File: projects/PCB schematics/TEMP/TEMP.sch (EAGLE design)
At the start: 58 parts, among them J1 SAMTEC-TFM-120-02-X-D-LCJ, J2 SAMTEC-TFM-120-02-X-D-LCJ, X1 5566-2, X2 5566-4, X3 5566-6, X4 5566-4

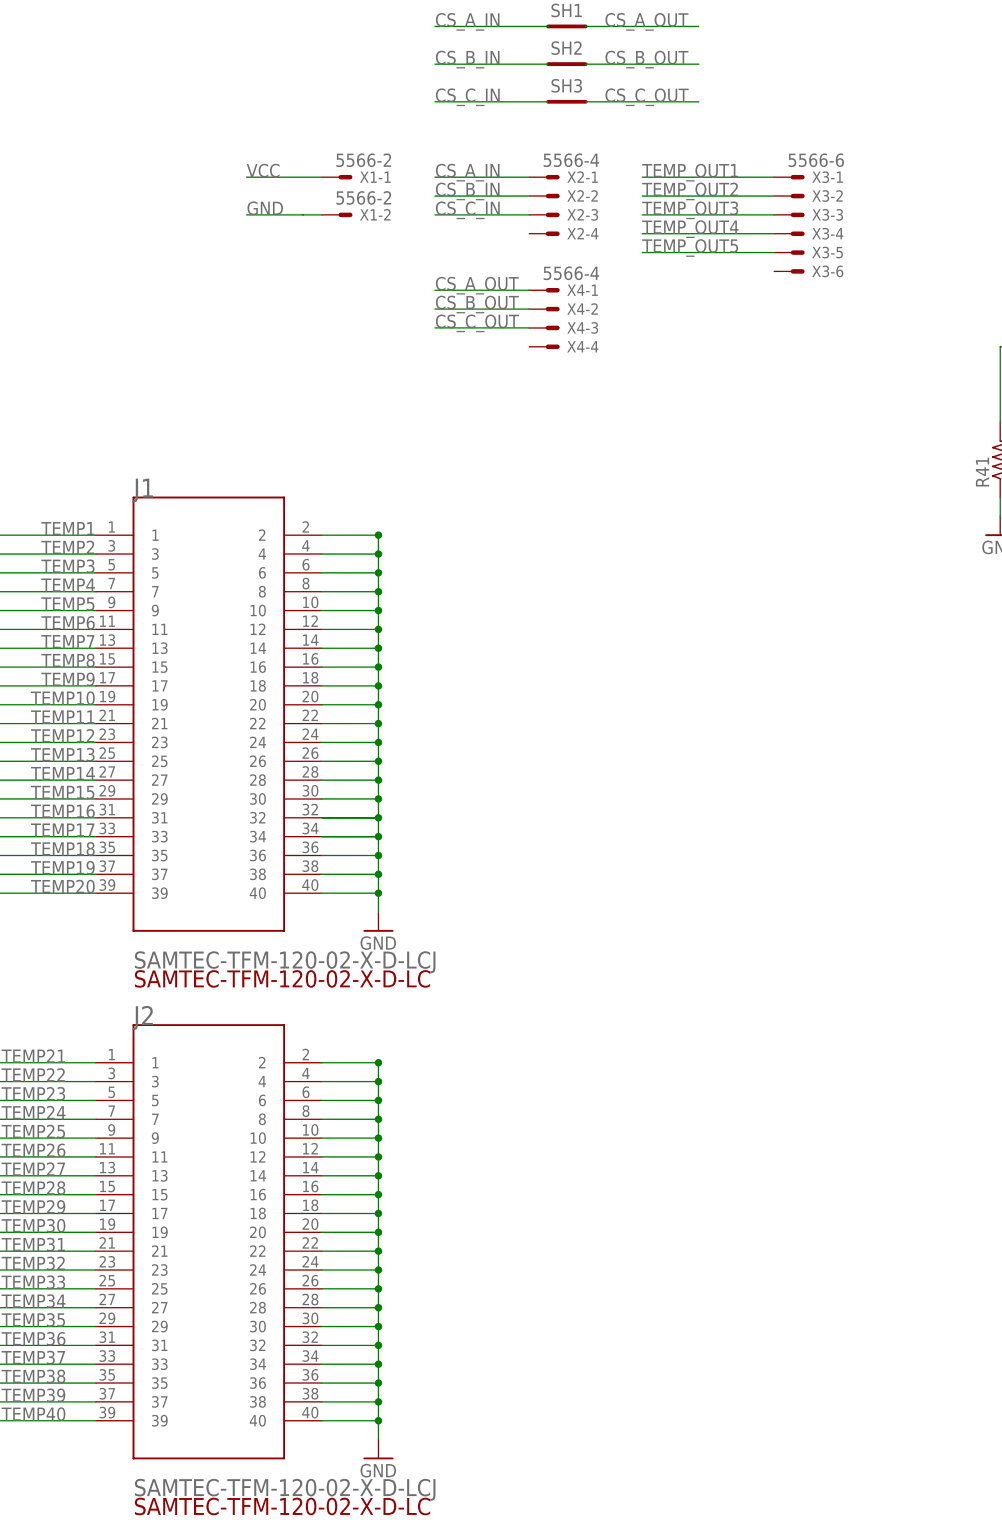
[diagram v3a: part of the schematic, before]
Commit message: TEMP - Initial board placement; Horizontal redo.
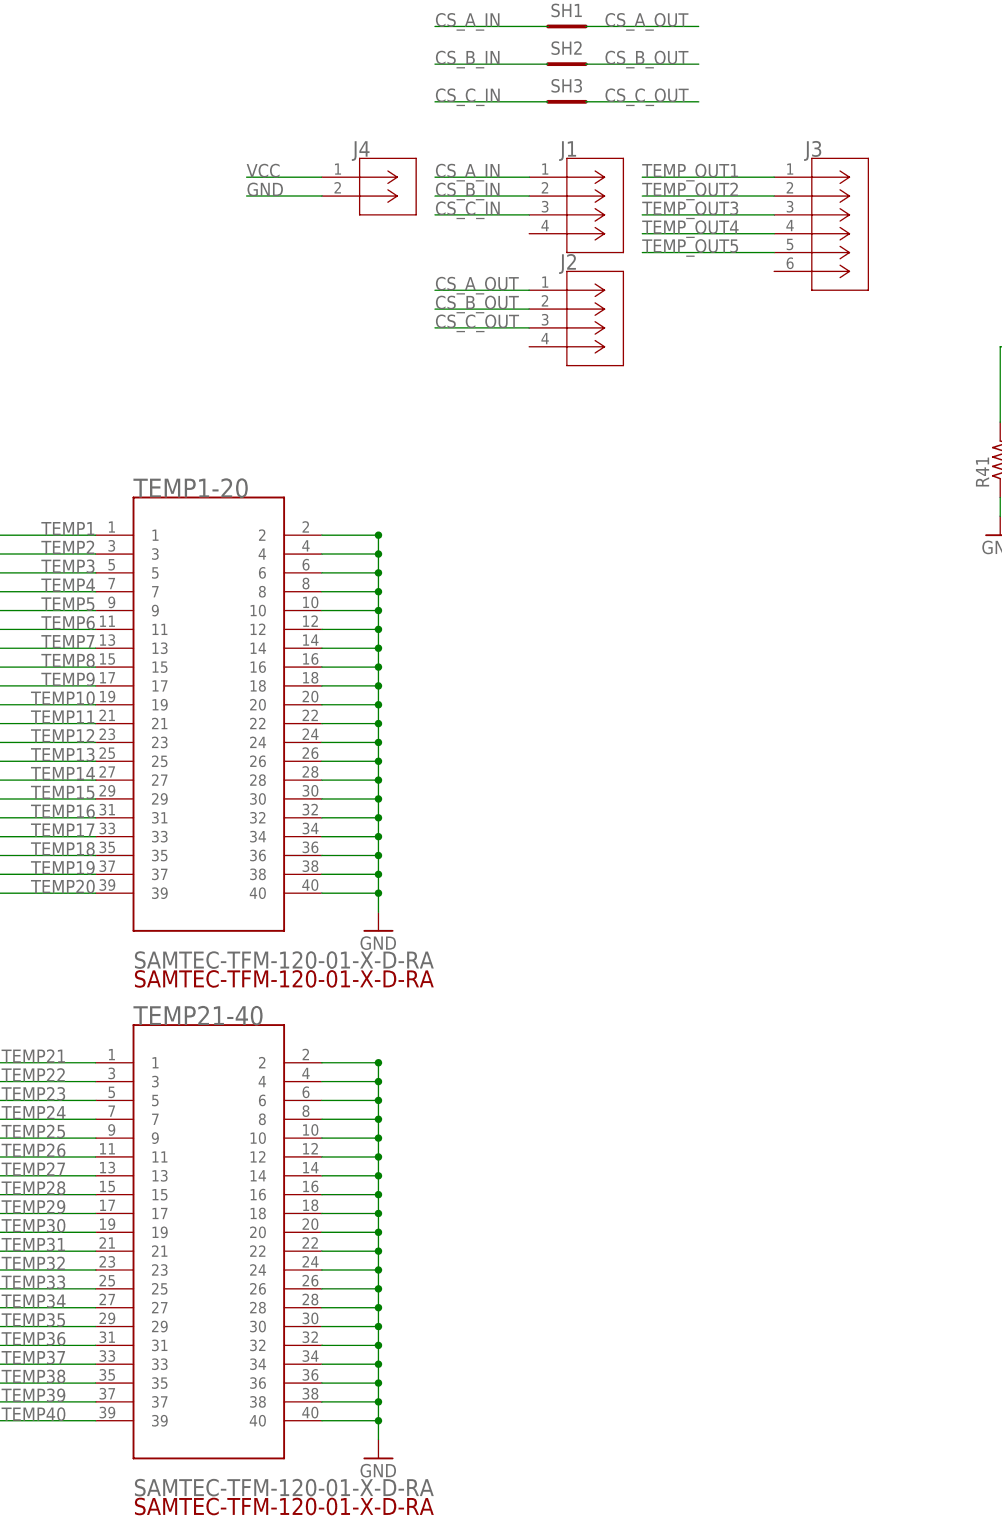
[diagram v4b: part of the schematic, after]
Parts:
- removed X1: 5566-2, con-molex:5566-2
- removed X2, X4: 5566-4, con-molex:5566-4
- removed X3: 5566-6, con-molex:5566-6
- added J3: 1-770969-0, IowaFormula:1-770969-0
- added J4: 770966-1, IowaFormula:770966-1
- added TEMP1-20, TEMP21-40: SAMTEC-TFM-120-01-X-D-RA, SAMTEC-TFM-120-01-X-D-RA:SAMTEC-TFM-120-01-X-D-RA
- J1, J2: value SAMTEC-TFM-120-02-X-D-LCJ -> 770968-1; device SAMTEC-TFM-120-02-X-D-LC:SAMTEC-TFM-120-02-X-D-LCJ -> IowaFormula:770968-1
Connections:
- net CS_A_IN: now also J1.1; no longer X2-1.S
- net CS_A_OUT: now also J2.1; no longer X4-1.S
- net CS_B_IN: now also J1.2; no longer X2-2.S
- net CS_B_OUT: now also J2.2; no longer X4-2.S
- net CS_C_IN: now also J1.3; no longer X2-3.S
- net CS_C_OUT: now also J2.3; no longer X4-3.S
- net GND: now also J4.2, TEMP1-20.10, TEMP1-20.12, TEMP1-20.14, TEMP1-20.16, TEMP1-20.18, TEMP1-20.2, TEMP1-20.20, TEMP1-20.22, TEMP1-20.24, TEMP1-20.26, TEMP1-20.28, TEMP1-20.30, TEMP1-20.32, TEMP1-20.34, TEMP1-20.36, TEMP1-20.38, TEMP1-20.4, TEMP1-20.40, TEMP1-20.6, TEMP1-20.8, TEMP21-40.10, TEMP21-40.12, TEMP21-40.14, TEMP21-40.16, TEMP21-40.18, TEMP21-40.2, TEMP21-40.20, TEMP21-40.22, TEMP21-40.24, TEMP21-40.26, TEMP21-40.28, TEMP21-40.30, TEMP21-40.32, TEMP21-40.34, TEMP21-40.36, TEMP21-40.38, TEMP21-40.4, TEMP21-40.40, TEMP21-40.6, TEMP21-40.8; no longer J1.10, J1.12, J1.14, J1.16, J1.18, J1.2, J1.20, J1.22, J1.24, J1.26, J1.28, J1.30, J1.32, J1.34, J1.36, J1.38, J1.4, J1.40, J1.6, J1.8, J2.10, J2.12, J2.14, J2.16, J2.18, J2.2, J2.20, J2.22, J2.24, J2.26, J2.28, J2.30, J2.32, J2.34, J2.36, J2.38, J2.4, J2.40, J2.6, J2.8, X1-2.S
- net TEMP1: now also TEMP1-20.1; no longer J1.1
- net TEMP10: now also TEMP1-20.19; no longer J1.19
- net TEMP11: now also TEMP1-20.21; no longer J1.21
- net TEMP12: now also TEMP1-20.23; no longer J1.23
- net TEMP13: now also TEMP1-20.25; no longer J1.25
- net TEMP14: now also TEMP1-20.27; no longer J1.27
- net TEMP15: now also TEMP1-20.29; no longer J1.29
- net TEMP16: now also TEMP1-20.31; no longer J1.31
- net TEMP17: now also TEMP1-20.33; no longer J1.33
- net TEMP18: now also TEMP1-20.35; no longer J1.35
- net TEMP19: now also TEMP1-20.37; no longer J1.37
- net TEMP2: now also TEMP1-20.3; no longer J1.3
- net TEMP20: now also TEMP1-20.39; no longer J1.39
- net TEMP21: now also TEMP21-40.1; no longer J2.1
- net TEMP22: now also TEMP21-40.3; no longer J2.3
- net TEMP23: now also TEMP21-40.5; no longer J2.5
- net TEMP24: now also TEMP21-40.7; no longer J2.7
- net TEMP25: now also TEMP21-40.9; no longer J2.9
- net TEMP26: now also TEMP21-40.11; no longer J2.11
- net TEMP27: now also TEMP21-40.13; no longer J2.13
- net TEMP28: now also TEMP21-40.15; no longer J2.15
- net TEMP29: now also TEMP21-40.17; no longer J2.17
- net TEMP3: now also TEMP1-20.5; no longer J1.5
- net TEMP30: now also TEMP21-40.19; no longer J2.19
- net TEMP31: now also TEMP21-40.21; no longer J2.21
- net TEMP32: now also TEMP21-40.23; no longer J2.23
- net TEMP33: now also TEMP21-40.25; no longer J2.25
- net TEMP34: now also TEMP21-40.27; no longer J2.27
- net TEMP35: now also TEMP21-40.29; no longer J2.29
- net TEMP36: now also TEMP21-40.31; no longer J2.31
- net TEMP37: now also TEMP21-40.33; no longer J2.33
- net TEMP38: now also TEMP21-40.35; no longer J2.35
- net TEMP39: now also TEMP21-40.37; no longer J2.37
- net TEMP4: now also TEMP1-20.7; no longer J1.7
- net TEMP40: now also TEMP21-40.39; no longer J2.39
- net TEMP5: now also TEMP1-20.9; no longer J1.9
- net TEMP6: now also TEMP1-20.11; no longer J1.11
- net TEMP7: now also TEMP1-20.13; no longer J1.13
- net TEMP8: now also TEMP1-20.15; no longer J1.15
- net TEMP9: now also TEMP1-20.17; no longer J1.17
- net TEMP_OUT1: now also J3.1; no longer X3-1.S
- net TEMP_OUT2: now also J3.2; no longer X3-2.S
- net TEMP_OUT3: now also J3.3; no longer X3-3.S
- net TEMP_OUT4: now also J3.4; no longer X3-4.S
- net TEMP_OUT5: now also J3.5; no longer X3-5.S
- net VCC: now also J4.1; no longer X1-1.S

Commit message: SC - Hand routing. Ready for autorouter.
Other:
- moved on the sheet: J1, J2, J3, J4, MUX1, MUX1P, MUX2, MUX2P, MUX3, MUX3P, MUX4, MUX4P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

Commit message: PROJ - Final pre-purchase revisions (4 boards still in progress.)
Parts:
- removed J2: 770968-1, IowaFormula:770968-1
- added CS.2: 770968-1, IowaFormula:770968-1
- renumbered J1 to CS.1, J3 to TEMP_OUT, J4 to VCC/GND
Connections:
- net CS_A_OUT: now also CS.2.1; no longer J2.1
- net CS_B_OUT: now also CS.2.2; no longer J2.2
- net CS_C_OUT: now also CS.2.3; no longer J2.3
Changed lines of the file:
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@@
 <part name="TEMP1-20" library="SAMTEC-TFM-120-01-X-D-RA" deviceset="SAMTEC-TFM-120-01-X-D-RA" device=""/>
 <part name="TEMP21-40" library="SAMTEC-TFM-120-01-X-D-RA" deviceset="SAMTEC-TFM-120-01-X-D-RA" device=""/>
-<part name="J1" library="IowaFormula" deviceset="770968-1" device=""/>
-<part name="J2" library="IowaFormula" deviceset="770968-1" device=""/>
-<part name="J3" library="IowaFormula" deviceset="1-770969-0" device=""/>
-<part name="J4" library="IowaFormula" deviceset="770966-1" device=""/>
+<part name="CS.1" library="IowaFormula" deviceset="770968-1" device=""/>
+<part name="CS.2" library="IowaFormula" deviceset="770968-1" device=""/>
+<part name="TEMP_OUT" library="IowaFormula" deviceset="1-770969-0" device=""/>
+<part name="VCC/GND" library="IowaFormula" deviceset="770966-1" device=""/>
 </parts>
 <sheets>
@@
 <attribute name="VALUE" x="50.8" y="7.62" size="2.286" layer="96"/>
 </instance>
-<instance part="J1" gate="A" x="132.08" y="119.38" smashed="yes">
+<instance part="CS.1" gate="A" x="132.08" y="119.38" smashed="yes">
 <attribute name="NAME" x="136.2456" y="122.1486" size="2.0828" layer="95" ratio="6" rot="SR0"/>
 </instance>
-<instance part="J2" gate="A" x="132.08" y="104.14" smashed="yes">
-<attribute name="NAME" x="136.2456" y="106.9086" size="2.0828" layer="95" ratio="6" rot="SR0"/>
-</instance>
-<instance part="J3" gate="A" x="165.1" y="119.38" smashed="yes">
-<attribute name="NAME" x="169.2656" y="122.1486" size="2.0828" layer="95" ratio="6" rot="SR0"/>
-</instance>
-<instance part="J4" gate="A" x="104.14" y="119.38" smashed="yes">
-<attribute name="NAME" x="108.3056" y="122.1486" size="2.0828" layer="95" ratio="6" rot="SR0"/>
+<instance part="CS.2" gate="A" x="132.08" y="101.6" smashed="yes">
+<attribute name="NAME" x="136.2456" y="104.3686" size="2.0828" layer="95" ratio="6" rot="SR0"/>
+</instance>
+<instance part="TEMP_OUT" gate="A" x="165.1" y="119.38" smashed="yes">
+<attribute name="NAME" x="166.7256" y="122.1486" size="2.0828" layer="95" ratio="6" rot="SR0"/>
+</instance>
+<instance part="VCC/GND" gate="A" x="104.14" y="119.38" smashed="yes">
+<attribute name="NAME" x="105.7656" y="122.1486" size="2.0828" layer="95" ratio="6" rot="SR0"/>
 </instance>
 </instances>
@@
 <wire x1="165.1" y1="119.38" x2="147.32" y2="119.38" width="0.1524" layer="91"/>
 <label x="147.32" y="119.38" size="1.778" layer="95"/>
-<pinref part="J3" gate="A" pin="1"/>
+<pinref part="TEMP_OUT" gate="A" pin="1"/>
 </segment>
 </net>
@@
 <wire x1="165.1" y1="116.84" x2="147.32" y2="116.84" width="0.1524" layer="91"/>
 <label x="147.32" y="116.84" size="1.778" layer="95"/>
-<pinref part="J3" gate="A" pin="2"/>
+<pinref part="TEMP_OUT" gate="A" pin="2"/>
 </segment>
 </net>
@@
 <wire x1="165.1" y1="114.3" x2="147.32" y2="114.3" width="0.1524" layer="91"/>
 <label x="147.32" y="114.3" size="1.778" layer="95"/>
-<pinref part="J3" gate="A" pin="3"/>
+<pinref part="TEMP_OUT" gate="A" pin="3"/>
 </segment>
 </net>
@@
 <wire x1="165.1" y1="111.76" x2="147.32" y2="111.76" width="0.1524" layer="91"/>
 <label x="147.32" y="111.76" size="1.778" layer="95"/>
-<pinref part="J3" gate="A" pin="4"/>
+<pinref part="TEMP_OUT" gate="A" pin="4"/>
 </segment>
 </net>
@@
 <wire x1="165.1" y1="109.22" x2="147.32" y2="109.22" width="0.1524" layer="91"/>
 <label x="147.32" y="109.22" size="1.778" layer="95"/>
-<pinref part="J3" gate="A" pin="5"/>
+<pinref part="TEMP_OUT" gate="A" pin="5"/>
 </segment>
 </net>
@@
 <wire x1="104.14" y1="119.38" x2="93.98" y2="119.38" width="0.1524" layer="91"/>
 <label x="93.98" y="119.38" size="1.778" layer="95"/>
-<pinref part="J4" gate="A" pin="1"/>
+<pinref part="VCC/GND" gate="A" pin="1"/>
 </segment>
 <segment>
@@
 <label x="93.98" y="116.84" size="1.778" layer="95"/>
 <wire x1="104.14" y1="116.84" x2="93.98" y2="116.84" width="0.1524" layer="91"/>
-<pinref part="J4" gate="A" pin="2"/>
+<pinref part="VCC/GND" gate="A" pin="2"/>
 </segment>
 <segment>
@@
 <net name="CS_A_OUT" class="0">
 <segment>
-<wire x1="132.08" y1="104.14" x2="119.38" y2="104.14" width="0.1524" layer="91"/>
-<label x="119.38" y="104.14" size="1.778" layer="95"/>
-<pinref part="J2" gate="A" pin="1"/>
+<wire x1="132.08" y1="101.6" x2="119.38" y2="101.6" width="0.1524" layer="91"/>
+<label x="119.38" y="101.6" size="1.778" layer="95"/>
+<pinref part="CS.2" gate="A" pin="1"/>
 </segment>
 <segment>
@@
 <wire x1="132.08" y1="119.38" x2="119.38" y2="119.38" width="0.1524" layer="91"/>
 <label x="119.38" y="119.38" size="1.778" layer="95"/>
-<pinref part="J1" gate="A" pin="1"/>
+<pinref part="CS.1" gate="A" pin="1"/>
 </segment>
 <segment>
@@
 <wire x1="119.38" y1="116.84" x2="132.08" y2="116.84" width="0.1524" layer="91"/>
 <label x="119.38" y="116.84" size="1.778" layer="95"/>
-<pinref part="J1" gate="A" pin="2"/>
+<pinref part="CS.1" gate="A" pin="2"/>
 </segment>
 <segment>
@@
 <wire x1="119.38" y1="114.3" x2="132.08" y2="114.3" width="0.1524" layer="91"/>
 <label x="119.38" y="114.3" size="1.778" layer="95"/>
-<pinref part="J1" gate="A" pin="3"/>
+<pinref part="CS.1" gate="A" pin="3"/>
 </segment>
 <segment>
@@
 </segment>
 <segment>
-<wire x1="119.38" y1="101.6" x2="132.08" y2="101.6" width="0.1524" layer="91"/>
-<label x="119.38" y="101.6" size="1.778" layer="95"/>
-<pinref part="J2" gate="A" pin="2"/>
+<wire x1="119.38" y1="99.06" x2="132.08" y2="99.06" width="0.1524" layer="91"/>
+<label x="119.38" y="99.06" size="1.778" layer="95"/>
+<pinref part="CS.2" gate="A" pin="2"/>
 </segment>
 </net>
@@
 </segment>
 <segment>
-<wire x1="119.38" y1="99.06" x2="132.08" y2="99.06" width="0.1524" layer="91"/>
-<label x="119.38" y="99.06" size="1.778" layer="95"/>
-<pinref part="J2" gate="A" pin="3"/>
-</segment>
-</net>
+<wire x1="119.38" y1="96.52" x2="132.08" y2="96.52" width="0.1524" layer="91"/>
+<label x="119.38" y="96.52" size="1.778" layer="95"/>
+<pinref part="CS.2" gate="A" pin="3"/>
+</segment>
+</net>
